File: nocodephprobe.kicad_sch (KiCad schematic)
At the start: 37 parts, among them J1 RF1-01 BNC, J2 10K, Q1 2N7002, SW1 SW_SPST, U1 LMV358a, U2 ICL7106CPL, U3 MCP1501T-10E/CHY, U4 VI-302-DP-RC-S, U5 78l05

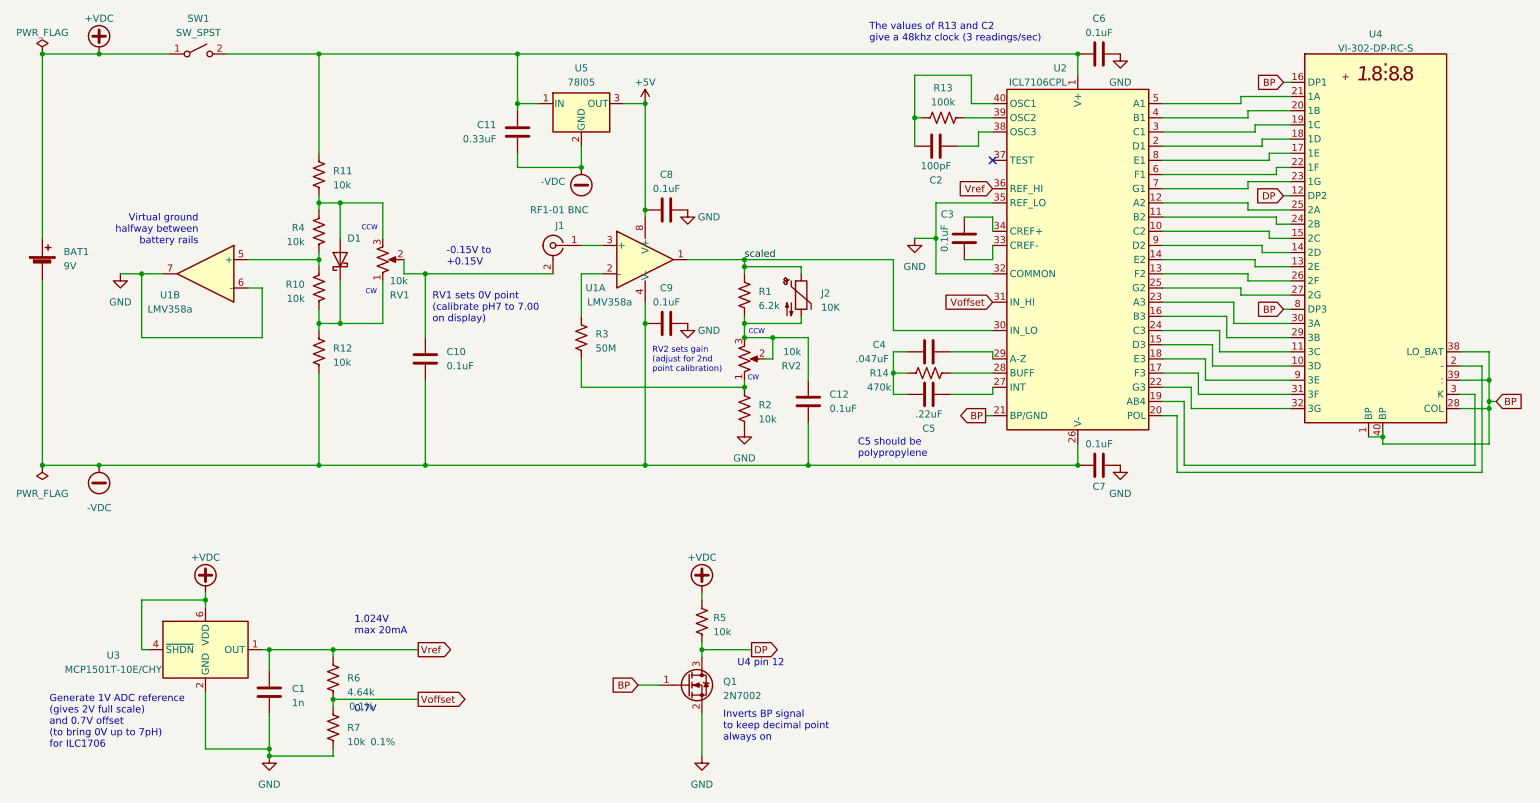
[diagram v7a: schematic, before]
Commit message: Regulate entire circuit to 5V
Though in the future I'd like to run the 7106 directly from the battery,
that requires centering the 7805 and lmv358a at the virtual ground.
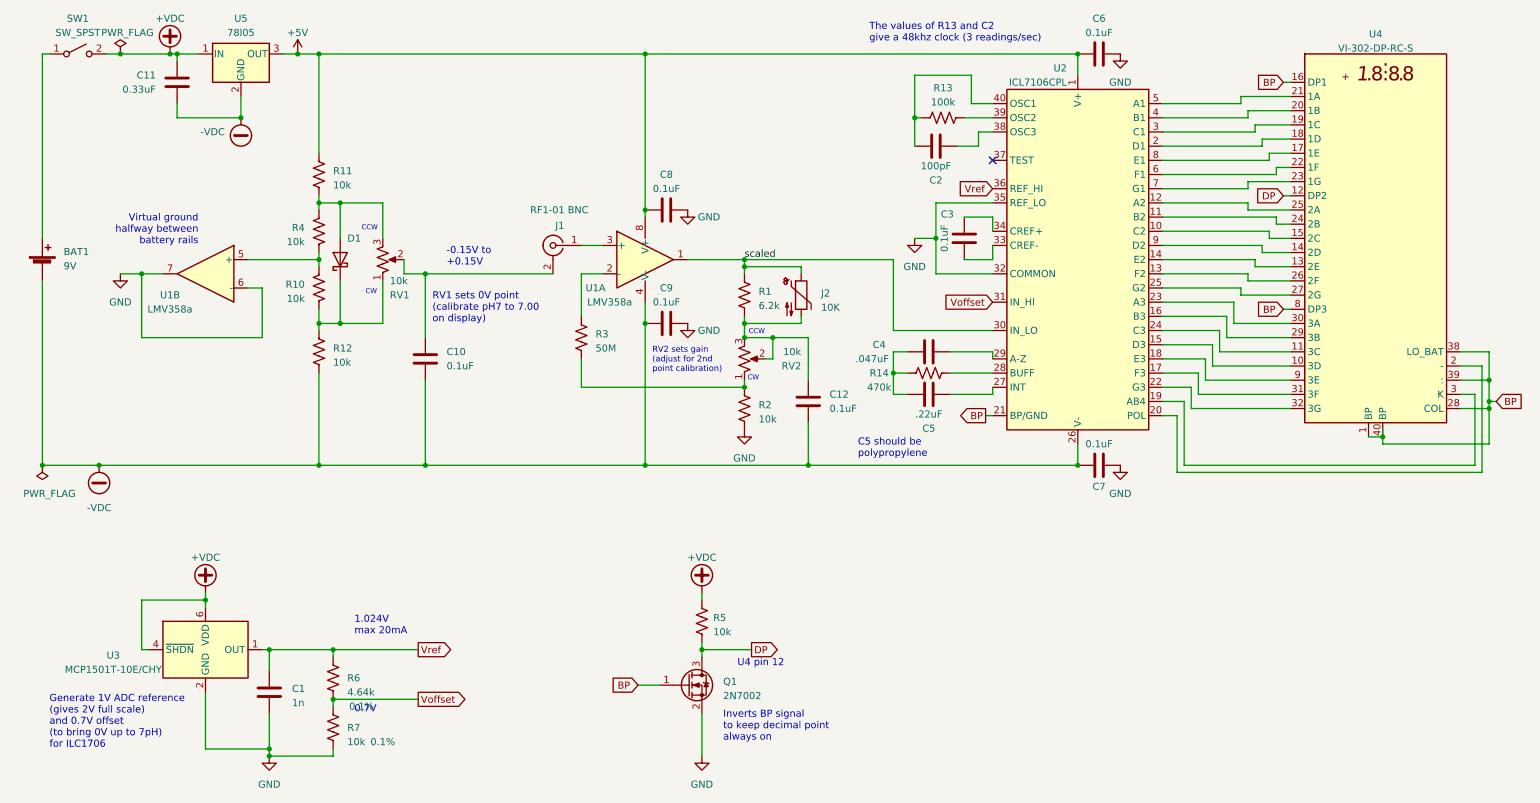
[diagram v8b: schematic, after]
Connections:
- net +5V: now also C6.1, R11.2, U2.1 (V+)
- net +VDC: now also C11.2, SW1.2 (B), U5.1 (IN); no longer BAT1.1 (+), SW1.1 (A)
- new net: BAT1.1 (+), SW1.1 (A)
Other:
- moved on the sheet: C11, SW1, U5
